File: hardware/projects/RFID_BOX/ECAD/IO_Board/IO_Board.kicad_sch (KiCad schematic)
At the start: 16 parts, among them J1 J_WAGO_2604-1103, J2 J_WAGO_2604-1103, J3 F_696309001002, K1 T92S11D12-24, K2 K_G5V-1-2_DC24, U1 ESP32-S3-WROOM-1, U2 PN5321A3HN_C1xx, U3 IC_IRM-10-24, U4 AMS1117-3.3, U5 IC_RFB-0505S, U6 MCP39F511A-E/MQ

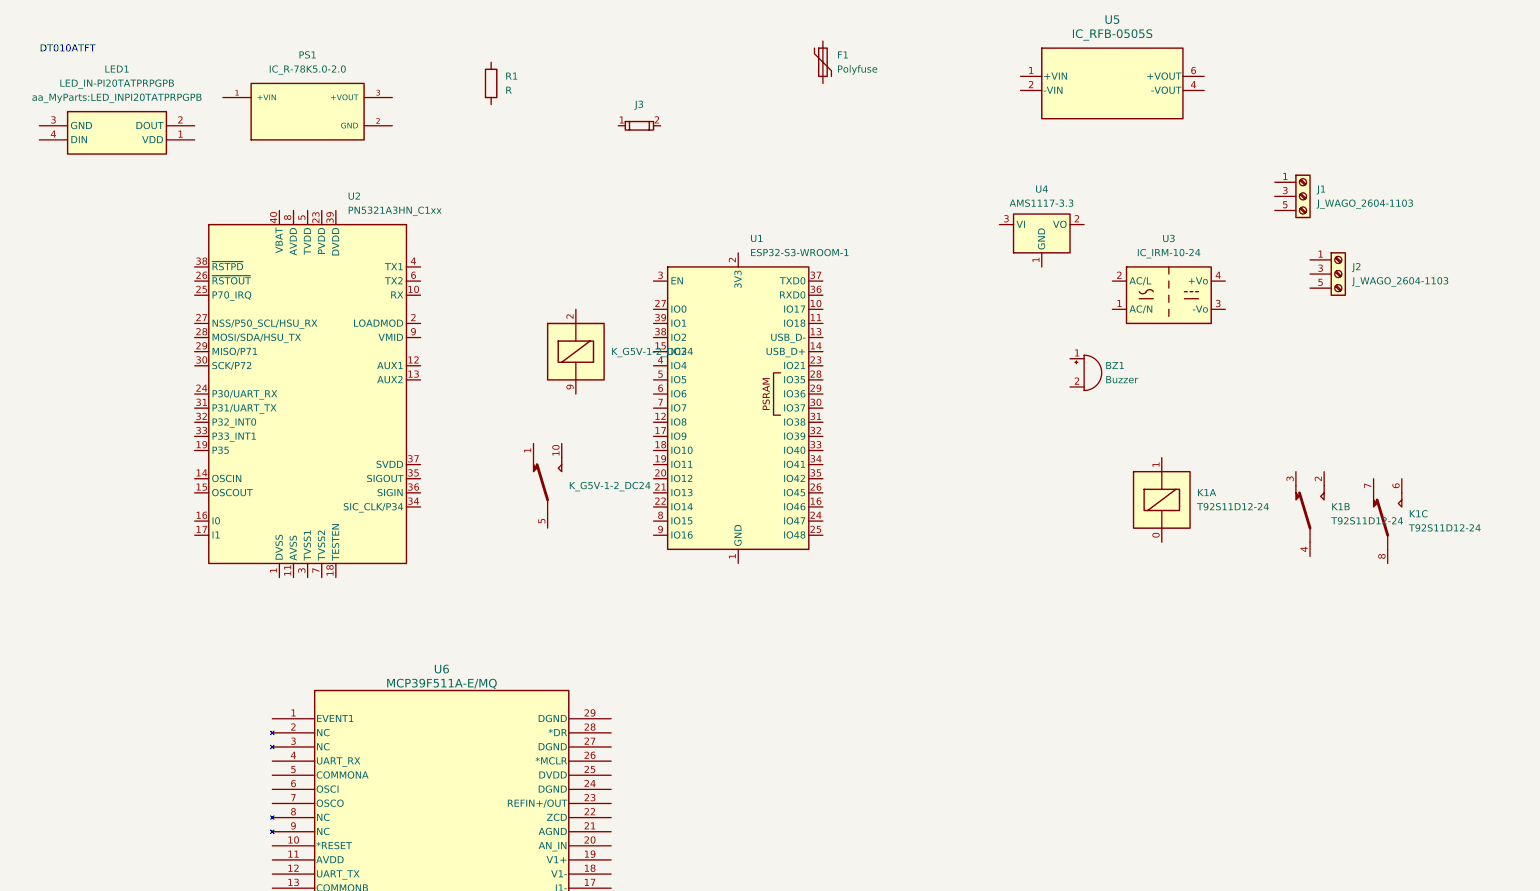
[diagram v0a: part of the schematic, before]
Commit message: Konkretisiere EMV-Bauteile und NTC in BOM, verschiebe PoC-KiCad-Projekt nach ECAD/IO_Board
- EMV Maßnahmen in Bauteilauswahl auf MOV, X2-Kondensator und Gleichtaktdrossel
  mit realen Herstellerteilen und Digikey-Bestellnummern aufgesplittet
- NTC von 10R/3.5A (zu gering für 8A Lastpfad) auf Bourns BN-LG15Y2R5MYB
  (2.5R/8A) korrigiert
- cad/PoC KiCad-Projekt nach ECAD/IO_Board umbenannt (laufender Layout-Fortschritt)
- .gitignore um Backup-Ordner des neuen ECAD-Pfads ergänzt
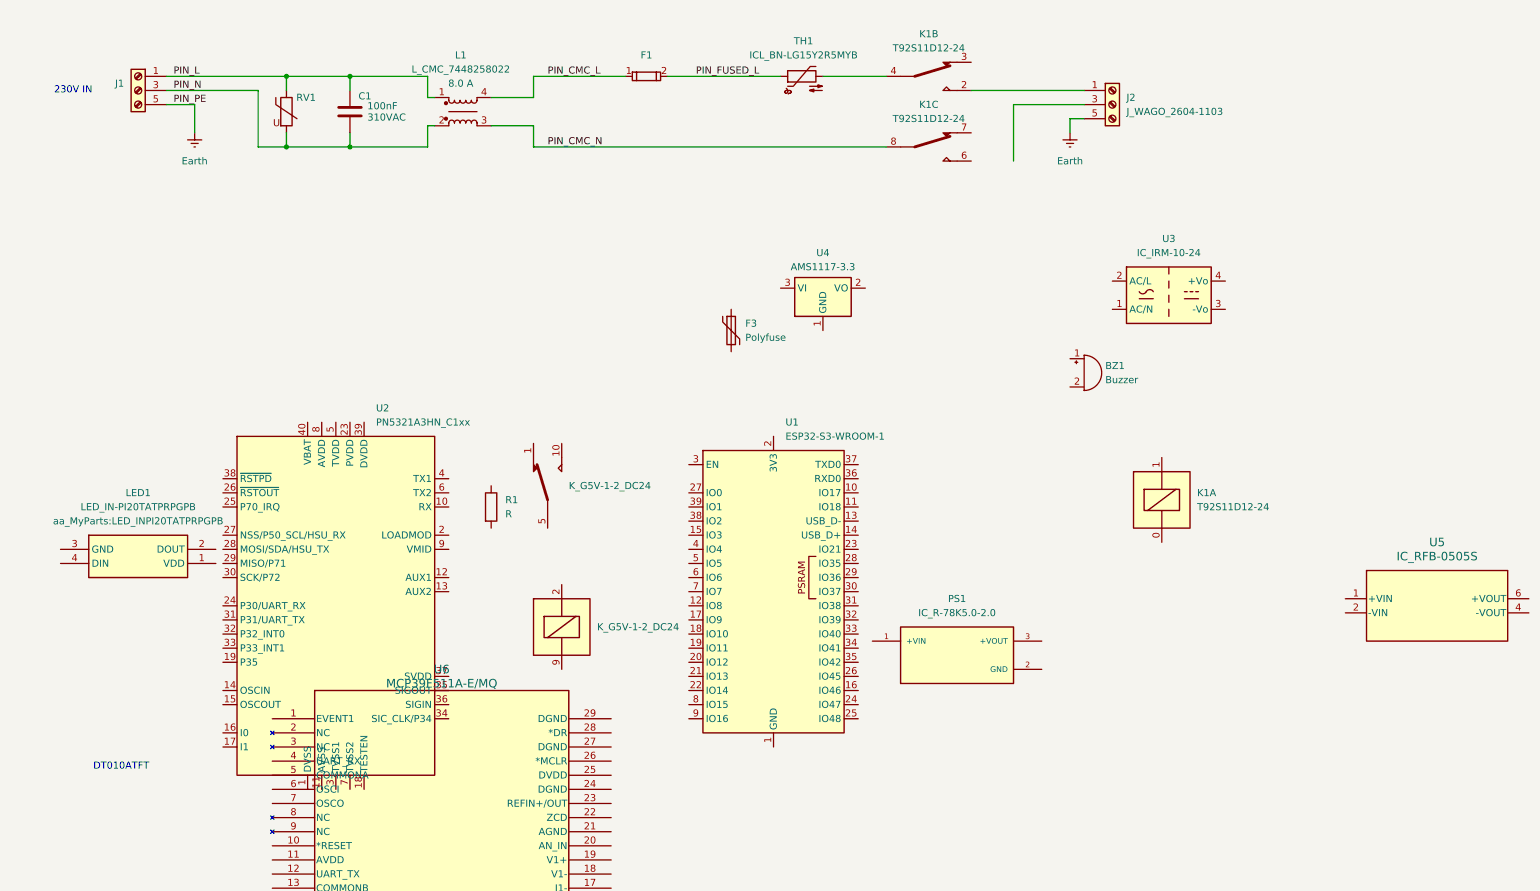
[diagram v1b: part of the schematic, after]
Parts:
- added C1: C_X2_890334023023CS, aa_MyParts:C_Wurth_WCAP-FTXX-P10L13W7H13, symbol aa_MyParts:C_X2_890334023023CS
- added L1: L_CMC_7448258022, aa_MyParts:L_Wurth_WE-CMB-XL, symbol aa_MyParts:L_CMC_7448258022
- added RV1: RVAR_B72210S0271K101, Varistor:RV_Disc_D12mm_W5.1mm_P7.5mm, symbol aa_MyParts:RVAR_B72210S0271K101
- added TH1: ICL_BN-LG15Y2R5MYB, Varistor:RV_Disc_D15.5mm_W8mm_P7.5mm, symbol aa_MyParts:ICL_BN-LG15Y2R5MYB
- renumbered J3 to F1, F1 to F3
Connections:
- net PIN_L: now reaches J1.1 (Pin_1), J1.2 (Pin_2)
- net PIN_L: now also C1.1, L1.1, RV1.1
- net PIN_N: now reaches J1.3 (Pin_3), J1.4 (Pin_4)
- net PIN_N: now also C1.2, L1.2, RV1.2
- net Earth: now reaches J1.5 (Pin_5), J1.6 (Pin_6)
- net Earth: now also J2.5 (Pin_5), J2.6 (Pin_6)
- net at J2.1 (Pin_1), J2.2 (Pin_2): now also K1.2
- net PIN_CMC_N: now reaches K1.8
- net PIN_CMC_N: now also L1.3
- net PIN_CMC_L: now reaches F1.1
- net PIN_CMC_L: now also L1.4
- net PIN_FUSED_L: now reaches F1.2
- net PIN_FUSED_L: now also TH1.1
- net at K1.4: now also TH1.2
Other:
- note added: "230V IN"
- moved on the sheet: F1, F3, J1, J2, K1B, K1C, LED1, PS1, R1, U1, U2, U4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

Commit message: Optokoppler auf Vishay VO615A-X017T (verstärkte Isolierung) umgestellt, IO-Board Layout-Fortschritt
- PC817 durch Vishay VO615A-X017T ersetzt: VDE 0884-5 zertifizierte verstärkte
  Isolierung passend zur restlichen Schutzklasse-II-Auslegung (Relais, IRM-10-24),
  da der Optokoppler die einzige Isolationsbarriere der Lastmessung ist
- IO_Board KiCad-Projekt: Platzierungs-Fortschritt
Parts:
- added F2: 1A 250VAC, aa_MyParts:F_MRT_BEL, symbol aa_MyParts:F_MRT 1-BULK
- added U7, U8: VO615A-1, Package_DIP:DIP-4_W7.62mm, symbol Isolator:VO615A-1
- R1: value R -> 20mR; footprint (none) -> Resistor_SMD:R_1206_3216Metric
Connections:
- net PIN_CMC_L: now also F2.1
- net PIN_CMC_N: now also U3.1 (AC/N)
- net at U6.12 (UART_TX): now also U7.2
- net at U6.17 (I1-): now also K1.4, R1.2
- net at U6.19 (V1+): now also R1.1, TH1.2
- net at U6.25 (DVDD): now also U4.2 (VO)
- net at U6.29 (DGND): now also U4.1 (GND), U5.4 (-VOUT)
- net at U6.4 (UART_RX): now also U8.2
- net at U4.3 (VI): now also U5.6 (+VOUT)
- net at U3.2 (AC/L): now also F2.2
- net at U3.3 (-Vo): now also U5.2 (-VIN)
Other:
- moved on the sheet: BZ1, C1, F1, F3, J1, J2, K1A, K1B, K1C, L1, LED1, PS1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
